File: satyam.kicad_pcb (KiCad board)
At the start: 2 copper layers, 47 x 41.9 mm, 4 parts, among them J1 Conn_01x02, U1 supermcu1

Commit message: PCB Layout
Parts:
- C1: value 10uF -> 30uF
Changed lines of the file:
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@@
       (effects (font (size 1 1) (thickness 0.15)))
     )
-    (fp_text value 10uF (at 0 1.65) (layer F.Fab)
+    (fp_text value 30uF (at 0 1.65) (layer F.Fab)
       (effects (font (size 1 1) (thickness 0.15)))
     )
@@
     (polygon
       (pts
-        (xy 167.64 107.95) (xy 120.65 107.95) (xy 120.65 66.04) (xy 167.64 66.04)
+        (xy 152.4635 91.313) (xy 120.65 91.44) (xy 120.523 73.66) (xy 152.3365 73.787)
       )
     )

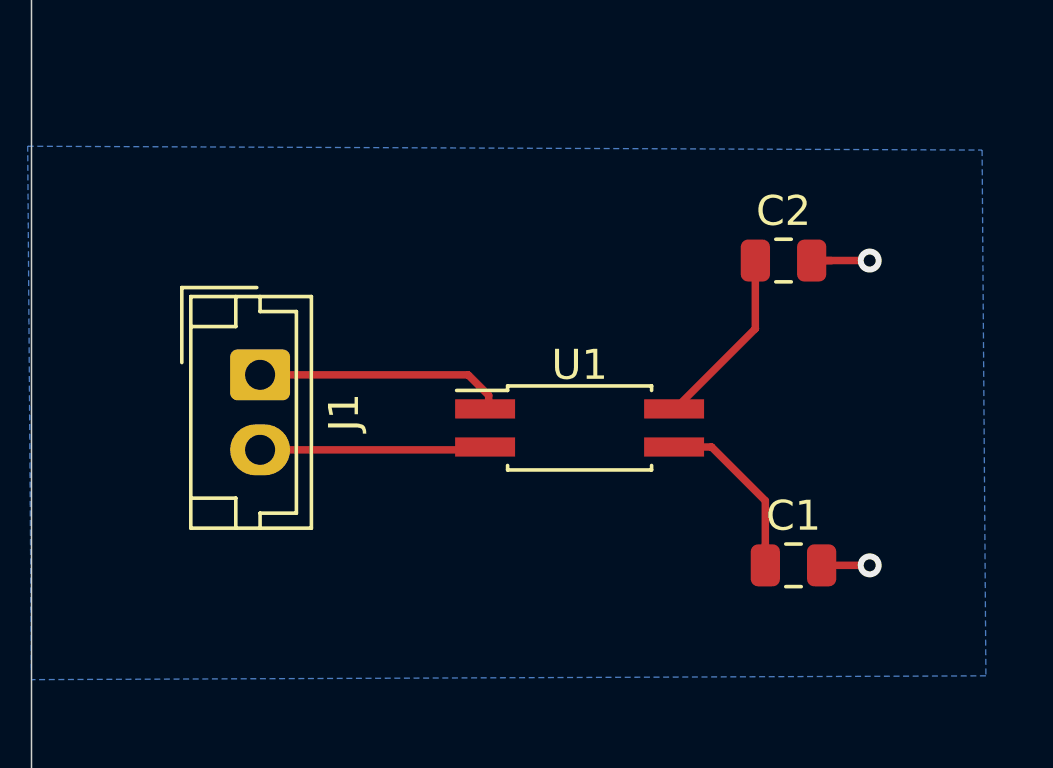
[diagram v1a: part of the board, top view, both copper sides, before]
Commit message: Components shifted to bottom
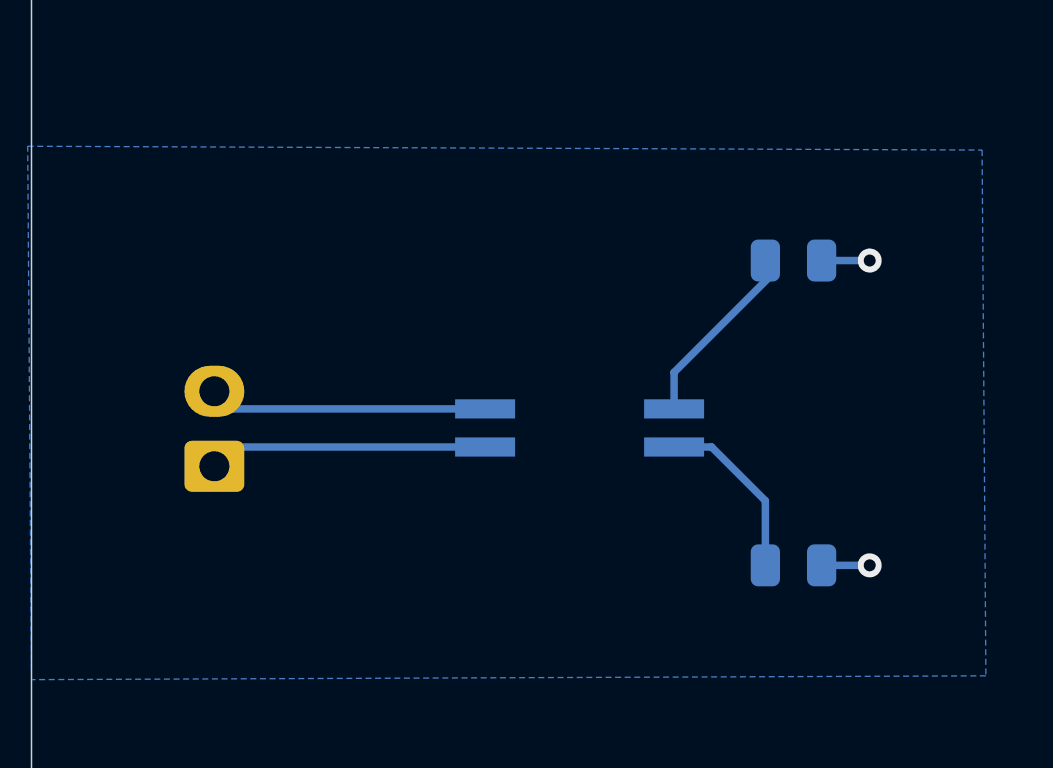
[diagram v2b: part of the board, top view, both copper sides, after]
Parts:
- C1, C2, J1, U1: moved to B.Cu
- moved C2 10.2 mm to (146.1, 87.6)
- moved C1 10.2 mm to (146.1, 77.5)
- moved J1 3.41 mm to (126.7, 84.3), turned to 90 degrees
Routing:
- net +3V3: track 8.40 -> 9.29 mm
- net GND: track 11.7 -> 12.5 mm
